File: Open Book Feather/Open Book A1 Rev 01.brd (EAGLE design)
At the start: 77.5 x 112.3 mm, 114 parts, among them J1 SJ-43514-SMT, J2 10118193-0001LF, Q1 DMG341, Q2 IRLML0100, SW1 SPDT_SWITCH, U1 AP2112-3.3, U2 MCP73831T-2ACI/OT, U3 ATSAMD51J64-TQFP(10X10), U4 GD25Q16C (or GD25Q32C), U5 74AC165D, U6 GD25Q16C (or GD25Q32C), U7 23K256-I/SN, X1 JSTPH, X2 2x5 0.05" SWD

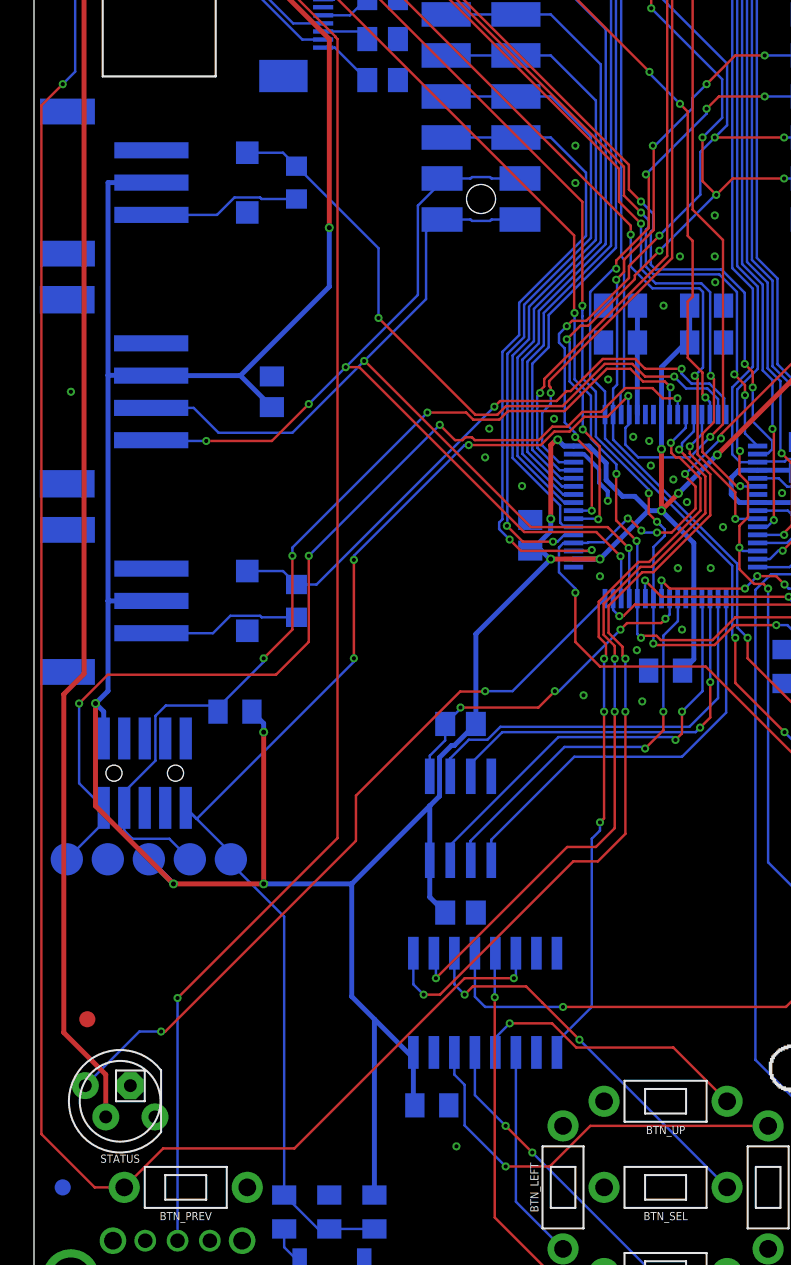
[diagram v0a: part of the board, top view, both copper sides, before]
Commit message: final version of open book A1-01 submitted to OSH Park
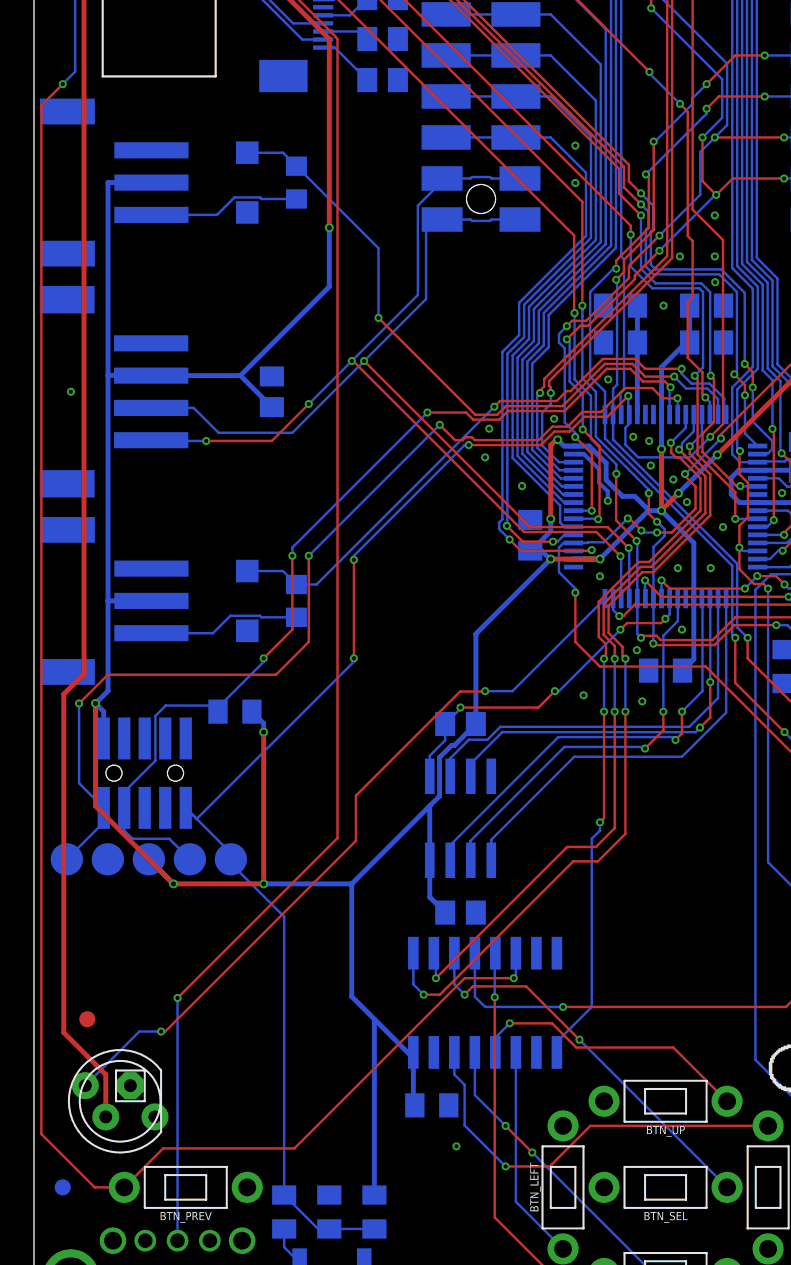
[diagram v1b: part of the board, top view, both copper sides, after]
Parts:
- moved U$44 0.38 mm to (26.9, 63.1)
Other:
- board text added: "C11 & C12 filter AVCC, isolated via FB1."
- board text added: "C5, C6, C7, C8: filtering caps on each power pin."
- board text added: "SAM D51 MICROCONTROLLER"
- board text removed: "20 Positive Source driving voltage 21 Power Supply pin for VGH and VSH 22 Negative Source driving voltage 23 Power Supply for VCOM, VGL & VSL 24 VCOM driving voltage"
- board text removed: ">1 NC 2 N-Channel MOSFET Gate Drive Control 3 Current Sense Input for Control Loop 4 Negative Gate driving voltage 5 Positive Gate driving voltage 6 Clock for external LM75 temp sensor 7 Data for external LM75 temp sensor 8 Bus selection pin (tied to GND) 9 Busy state output pin (EBSY) 10 Reset (ERST) 11 Data / Command input pin (EDC) 12 Chip Select input pin (ECS) 13 Serial clock pin (SPI: SCK) 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"
- board text removed: "Almost all pins are available for use by wings. A0 & A1 are used for the headphone jack's audio out, and the SPI pins are shared with the Unifont chip and SD card. Other than that, they're all free. Note that I2C pins do not have pull- up resistors on board."
- board text removed: "C5, C6, C7, C8: filtering caps on each power pin. C11 & C12 filter AVCC, isolated using FB1."
- board text removed: "FEATHER CONNECTOR!"
- board text removed: "NC"
- board text removed: "SAMD51 MICROCONTROLLER"
- board text removed: "The e-paper panel has an on-board booster that generates the high(er) voltages needed to drive the display. The circuit on the left deals with the boost voltages. C10-C16 are filtering caps for the power pins (in and out)."
